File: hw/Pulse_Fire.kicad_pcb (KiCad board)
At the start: 2 copper layers, 60 x 60 mm, 31 parts, among them J2 Conn_01x04, Q1 AO3400A, Q2 AO3400A, Q3 AO3400A, U1 PY32F003F18U6, U2 SC7A20, U3 FM8002A, U4 ME6206A33XG, U6 ME2188A50

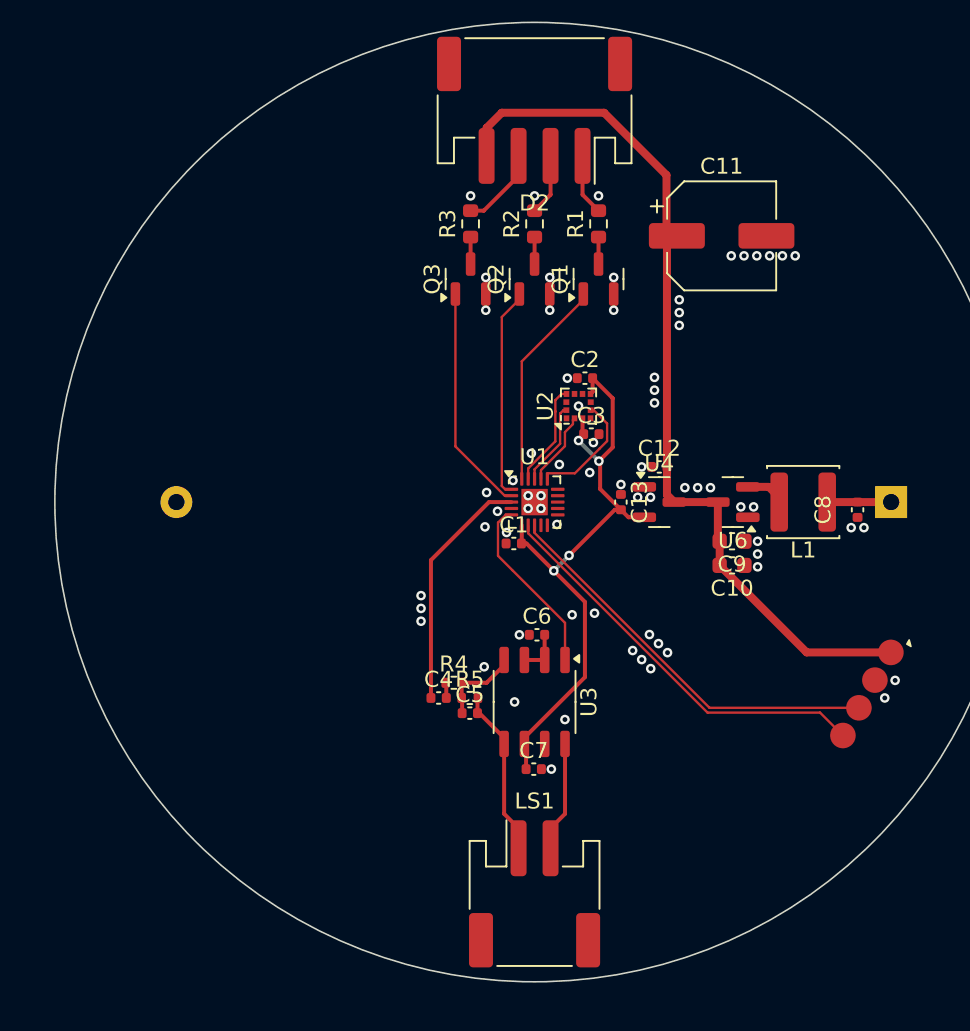
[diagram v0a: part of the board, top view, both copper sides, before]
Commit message: hw: Place silkscreen
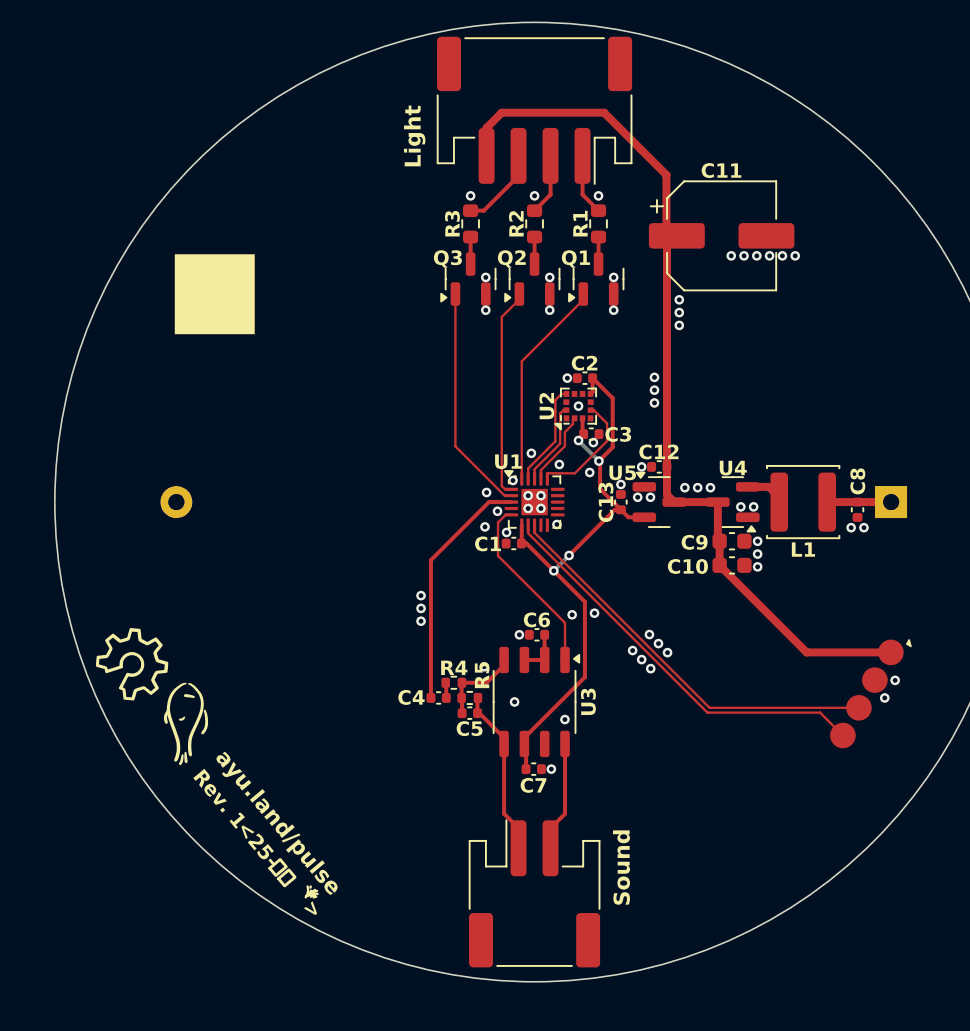
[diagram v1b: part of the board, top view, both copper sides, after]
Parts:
- added G***: LOGO, LOGO, F.Cu at (128.1, 113.9)
- added G***: LOGO, LOGO, F.Cu at (125.0, 110.0)
- renumbered D2 to D1, J2 to J1, U6 to U4, U4 to U5
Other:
- board text added: "<25-"
- board text added: ">"
- board text added: "Light"
- board text added: "Rev. 1"
- board text added: "Sound"
- board text added: "ayu.land/pulse"
- board text added: "ayu.land/pulse?id=F1_xx"
- board text added: "立秋"

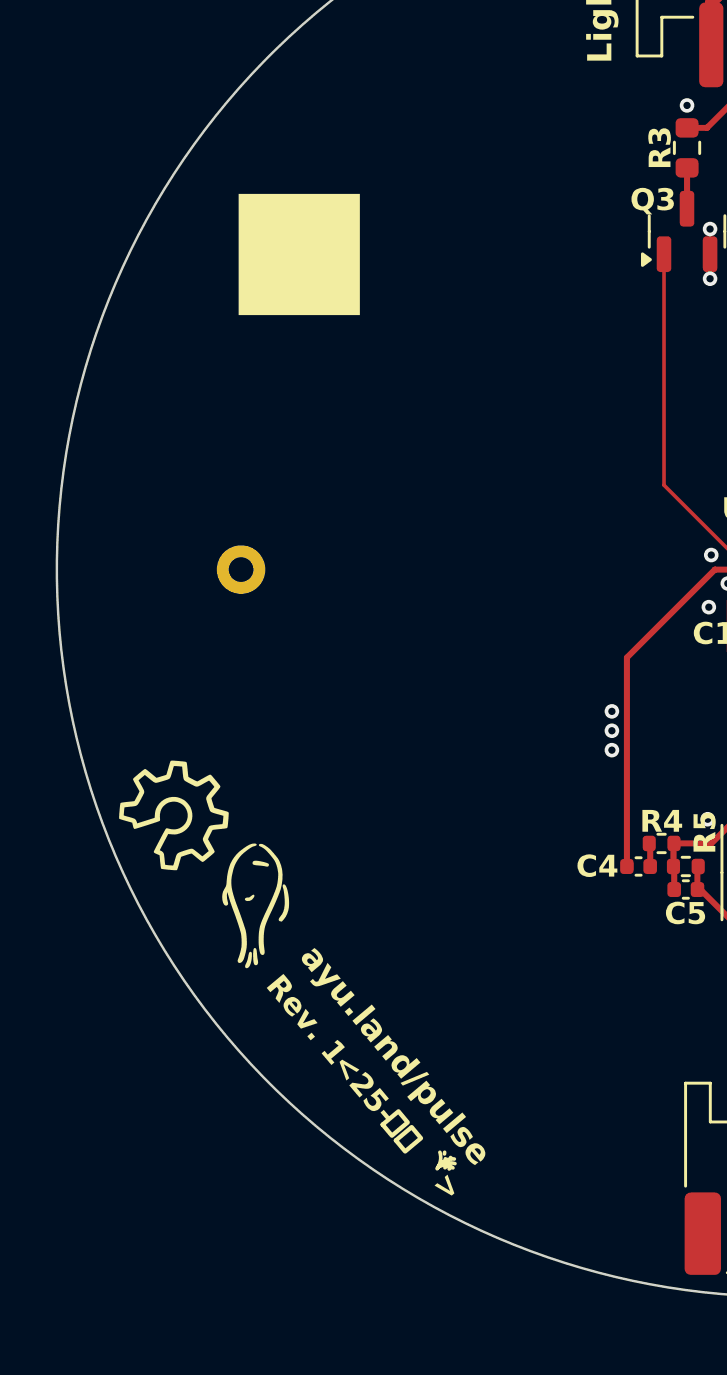
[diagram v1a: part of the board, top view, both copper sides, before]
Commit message: hw: Embed fonts; revise silkscreen
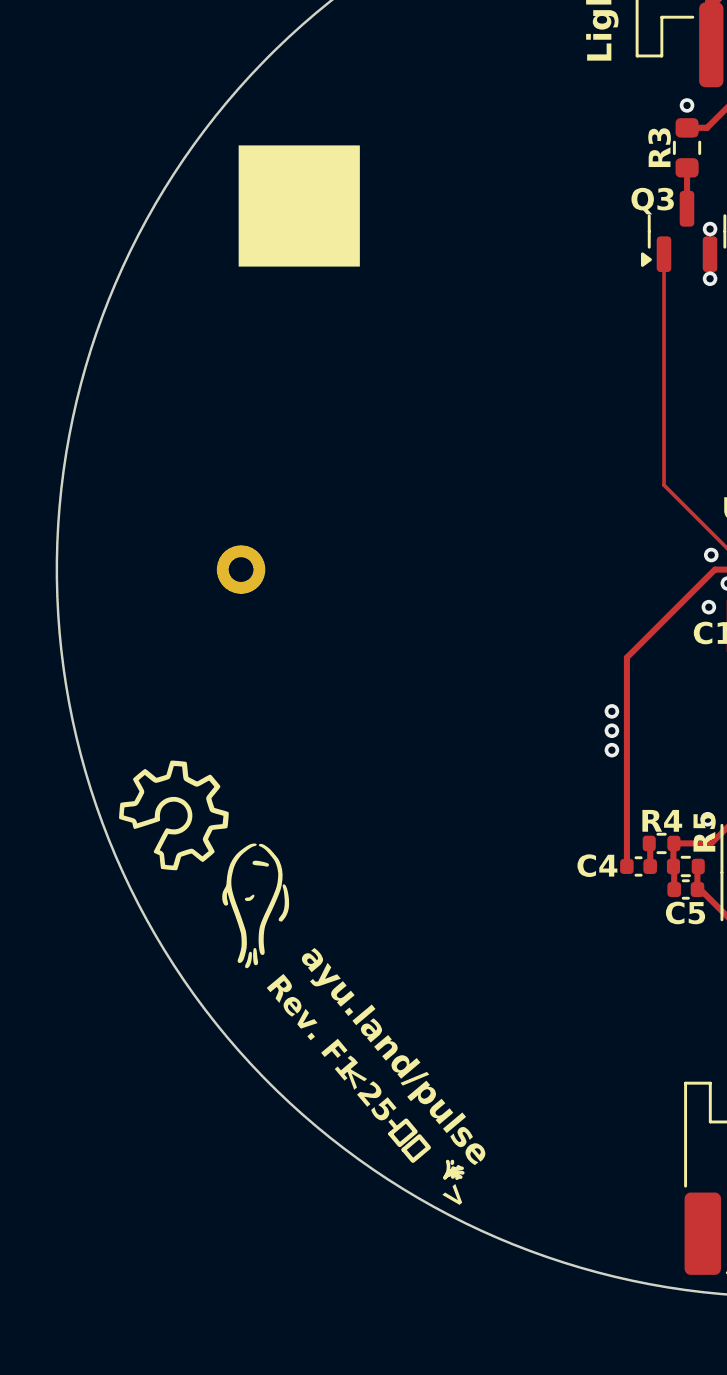
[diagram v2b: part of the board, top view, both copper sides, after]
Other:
- board text added: "Rev. F1"
- board text removed: "Rev. 1"
